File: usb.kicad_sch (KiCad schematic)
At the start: 22 parts, among them Q1 MMBT3904-C20526, Q2 MMBT3904-C20526, SW1 TS-1088-AR02016, U1 CP2102N-A02-GQFN24R

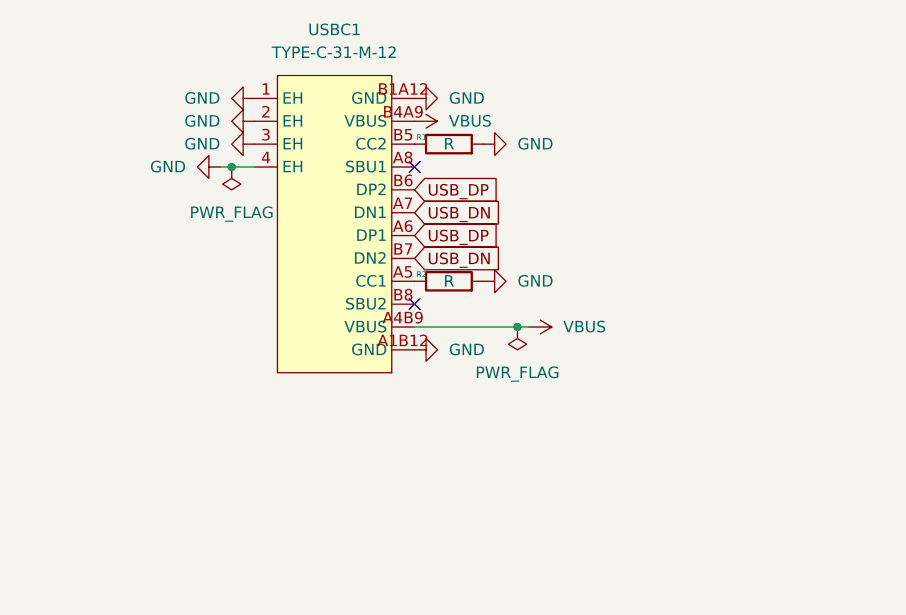
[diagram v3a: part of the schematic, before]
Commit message: Schematic and parts for enclosure B
- jack PJ-342C CB (TRRS, sinking) as CN1, HP-DET on JACK_SW, MIC to GND,
  100nF on JACK_DET (detect is now active low)
- USB-C TYPE-C 16P CB0.8 073 (sinking, 0.8 mm board) as USB1
- BT1 on JST SH SM02B-SRSS-TB, click wheel on TS-1187B-B (0.75 mm),
  power on EVQP7J01P side switch
- new footprints/3D models in lib; switch and JST SH footprints renumbered
  so the existing 2-pin symbols fit
- enclosure: power key on the right side, level with the display
- docs: connections.md, code.md and BOM updated

ERC: 0 errors, 0 warnings.

Co-Authored-By: Claude Opus 5.5 <noreply@anthropic.com>
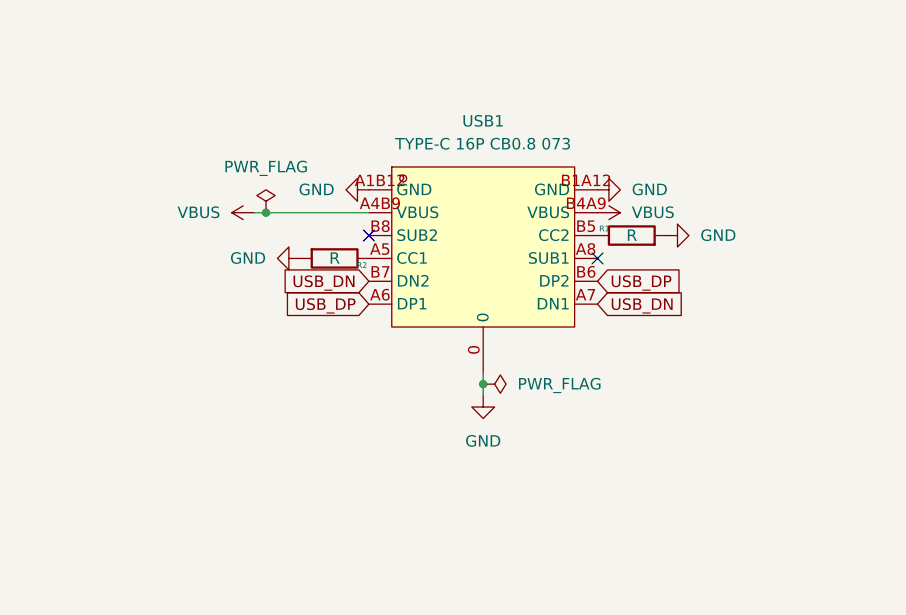
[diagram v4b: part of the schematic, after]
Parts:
- removed USBC1: TYPE-C-31-M-12, mp3_player:USB-C_SMD-TYPE-C-31-M-12_1, symbol mp3_player:TYPE-C-31-M-12
- added USB1: TYPE-C 16P CB0.8 073, mp3_player:USB-C-SMD_TYPE-C-16P-CB0.8-073, symbol mp3_player:TYPE-C16PCB0.8073
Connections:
- net GND: now also USB1.0, USB1.A1B12 (GND), USB1.B1A12 (GND)
- net USB_DN: now also USB1.A7 (DN1), USB1.B7 (DN2)
- net USB_DP: now also USB1.A6 (DP1), USB1.B6 (DP2)
- net VBUS: now also USB1.A4B9 (VBUS), USB1.B4A9 (VBUS)
- net at R2.1: now also USB1.A5 (CC1)
- net at R1.1: now also USB1.B5 (CC2)
